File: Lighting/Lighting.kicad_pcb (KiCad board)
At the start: 2 copper layers, 70 x 65 mm, 72 parts, among them J1 USB_C_Receptacle, J2 USB_C_Receptacle, Q1 PSMN011, U1 MCP2210T-I_SO, U2 UTC2000-I_MG, U3 DAC8551IDGKT, U5 MCP1501_2v5, Y1 Crystal_12MHz

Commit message: gerber zip looks good to me
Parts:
- moved TP3 0.90 mm to (231.1, 120.9)
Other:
- board text added: "GND"
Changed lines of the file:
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@@
   (general
     (thickness 1.6)
-    (drawings 11)
+    (drawings 15)
     (tracks 567)
     (zones 0)
@@
   )
   (setup
-    (last_trace_width 0.25)
+    (last_trace_width 1.016)
     (user_trace_width 0.1524)
     (user_trace_width 0.2032)
@@
     (visible_elements 7FFFFFFF)
     (pcbplotparams
-      (layerselection 0x01000_7fffffff)
+      (layerselection 0x010f0_ffffffff)
       (usegerberextensions false)
       (usegerberattributes false)
@@
       (padsonsilk false)
       (subtractmaskfromsilk false)
-      (outputformat 4)
+      (outputformat 1)
       (mirror false)
-      (drillshape 2)
+      (drillshape 0)
       (scaleselection 1)
       (outputdirectory "Lighting_Fab/"))
@@
   (module wsolar:LED0805 (layer F.Cu)
     (at 237.758967 68.854171 90)
-    (fp_text reference D8 (at 0 -2.167 90) (layer F.SilkS)
+    (fp_text reference D8 (at -2.773829 -0.014967 180) (layer F.SilkS)
       (effects (font (size 1 1) (thickness 0.15)))
     )
@@
   (module wsolar:jumper_2 (layer F.Cu)
     (at 236.22 119.38)
-    (fp_text reference JP2 (at 0.635 2.54) (layer F.SilkS)
+    (fp_text reference JP2 (at 0 2.032) (layer F.SilkS)
       (effects (font (size 1 1) (thickness 0.15)))
     )
@@
   )
   (module wsolar:TP (layer F.Cu)
-    (at 232.029 120.777)
+    (at 231.14 120.904)
     (fp_text reference TP3 (at 0 -1.905) (layer F.SilkS)
       (effects (font (size 1 1) (thickness 0.15)))
@@
     (pad 20 smd rect (at 4.6 -5.715) (size 1.9 0.6) (layers F.Cu F.Paste F.Mask)
       (net 1 GND))
+  )
+  (gr_text GND (at 233.68 64.008 90) (layer F.SilkS)
+    (effects (font (size 1.27 1.27) (thickness 0.254)))
+  )
+  (gr_text GND (at 205.74 102.108) (layer F.SilkS)
+    (effects (font (size 1.5 1.5) (thickness 0.3)))
+  )
+  (gr_text GND (at 232.156 123.444) (layer F.SilkS)
+    (effects (font (size 1.27 1.27) (thickness 0.254)))
+  )
+  (gr_text GND (at 220.98 76.2) (layer F.SilkS)
+    (effects (font (size 1.5 1.5) (thickness 0.3)))
   )
   (gr_text "Wellesley Solar: Lighting Module v1" (at 233.68 92.583 45) (layer B.SilkS)
@@
   (segment (start 235.7374 81.805) (end 231.9214 81.805) (width 1.016) (layer F.Cu) (net 5))
   (segment (start 231.9214 81.805) (end 227.2534 86.473) (width 1.016) (layer F.Cu) (net 5))
-  (segment (start 235.7374 79.8322) (end 235.7374 81.805) (width 0.254) (layer F.Cu) (net 5))
-  (segment (start 229.3874 78.74) (end 234.6452 78.74) (width 0.254) (layer F.Cu) (net 5))
-  (segment (start 234.6452 78.74) (end 235.7374 79.8322) (width 0.254) (layer F.Cu) (net 5))
   (segment (start 235.218967 70.851033) (end 234.2388 71.8312) (width 0.254) (layer F.Cu) (net 5))
   (segment (start 235.218967 69.870171) (end 235.218967 70.851033) (width 0.254) (layer F.Cu) (net 5))
@@
   (segment (start 226.6696 78.232) (end 227.1776 78.74) (width 0.254) (layer F.Cu) (net 5))
   (segment (start 227.1776 78.74) (end 229.3874 78.74) (width 0.254) (layer F.Cu) (net 5))
+  (segment (start 229.3874 78.74) (end 234.6452 78.74) (width 1.016) (layer F.Cu) (net 5))
+  (segment (start 234.6452 78.74) (end 235.7374 79.8322) (width 1.016) (layer F.Cu) (net 5))
+  (segment (start 235.7374 79.8322) (end 235.7374 81.805) (width 1.016) (layer F.Cu) (net 5))
   (segment (start 247.019 105.1) (end 247.8532 105.9342) (width 0.254) (layer F.Cu) (net 6))
   (segment (start 246.04 105.1) (end 247.019 105.1) (width 0.254) (layer F.Cu) (net 6))
@@
     (polygon
       (pts
-        (xy 224.155 113.03) (xy 231.14 113.03) (xy 232.41 114.3) (xy 232.41 115.57) (xy 229.87 118.11)
-        (xy 229.7176 122.4788) (xy 224.0026 122.4788)
+        (xy 224.155 113.03) (xy 231.14 113.03) (xy 232.664 114.3) (xy 232.664 115.824) (xy 232.664 118.364)
+        (xy 232.664 122.428) (xy 224.0026 122.4788)
       )
     )

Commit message: changes based on feedback
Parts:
- removed C8: C_0u1, wsolar:C_0805
- removed D3, D4: LED_645nm, wsolar:LED0805
- removed JP4: Jumper_NO_Small, wsolar:jumper_2
- removed R10, R12, R8, R9: R_1k, wsolar:R0805
- removed R14, R15, R6, R7: R_10k, wsolar:R0805
- removed R17: R_39k4, wsolar:R0805
- removed U2: UTC2000-I_MG, wsolar:QFN50P300X300X90-17N
- D1, D2: value LED_645nm -> D_Zener_5v6; footprint wsolar:LED0805 -> wsolar:SOD123
- J2: value USB_C_Receptacle -> USB_B_Micro; footprint wsolar:MOLEX_105450-0101 -> wsolar:FCI_10118193-0001LF
- JP3: value Jumper_NO_Small -> Jumper_3; footprint wsolar:jumper_2 -> wsolar:jumper_3
- R4: value R_35k7 -> R_10k
- R5: value R_5k1 -> R_39k2
- U3: value DAC8551IDGKT -> DAC6551AQDGKRQ1; footprint wsolar:S-PDSO-G8 -> wsolar:SOP65P490X110-9N
- U4: value (none) -> LMC6482
- moved TP1 61.8 mm to (260.6, 70.6)
- moved D2 49.2 mm to (229.7, 105.3)
- moved R5 41.7 mm to (237.4, 117.9), turned to 180 degrees
- moved TP4 39.7 mm to (260.6, 78.1)
- moved TP2 32.2 mm to (260.6, 85.3)
- moved R4 29.9 mm to (237.6, 106.5), turned to 270 degrees
- moved D1 24.6 mm to (261.8, 101.6), turned to 90 degrees
- moved JP1 22.3 mm to (227.8, 96.0), turned to 270 degrees
- moved R1 19.0 mm to (231.8, 99.7)
- moved TP3 18.0 mm to (249.2, 121.2)
- moved R3 16.9 mm to (245.0, 70.6), turned to 270 degrees
- moved C5 13.6 mm to (251.3, 100.3), turned to 270 degrees
- moved R11 11.6 mm to (224.2, 77.5), turned to 0 degrees
- moved C9 7.53 mm to (248.9, 108.5), turned to 0 degrees
- moved R16 7.03 mm to (256.5, 101.6)
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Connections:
- D1 pad 2: Net-(D1-Pad2) -> GND
- D2 pad 2: Net-(D2-Pad2) -> GND
- J1 pad A10: Net-(J1-PadA10) -> (no net)
- J1 pad A11: Net-(J1-PadA11) -> (no net)
- J1 pad A2: Net-(J1-PadA2) -> (no net)
- J1 pad A3: Net-(J1-PadA3) -> (no net)
- J1 pad A6: Net-(J1-PadA6) -> (no net)
- J1 pad A7: Net-(J1-PadA7) -> (no net)
- J1 pad A8: Net-(J1-PadA8) -> (no net)
- J1 pad B10: Net-(J1-PadB10) -> (no net)
- J1 pad B11: Net-(J1-PadB11) -> (no net)
- J1 pad B2: Net-(J1-PadB2) -> (no net)
- J1 pad B3: Net-(J1-PadB3) -> (no net)
- J1 pad B6: Net-(J1-PadB6) -> (no net)
- J1 pad B7: Net-(J1-PadB7) -> (no net)
- J1 pad B8: Net-(J1-PadB8) -> (no net)
- JP3 pad 1: Net-(JP3-Pad1) -> Net-(D2-Pad1)
- R16 pad 2: Net-(J2-PadA4) -> Net-(D1-Pad1)
- R2 pad 1: Net-(J1-PadA5) -> Net-(J1-PadB5)
- R3 pad 1: Net-(J1-PadB5) -> Net-(J1-PadA5)
- R4 pad 1: Net-(C6-Pad1) -> Net-(JP3-Pad2)
- R4 pad 2: Net-(R4-Pad2) -> GND
- R5 pad 1: Net-(R4-Pad2) -> VCC
- R5 pad 2: GND -> Net-(JP2-Pad1)
- RV1 pad 2: Net-(JP3-Pad1) -> Net-(JP3-Pad3)
- TP3 pad 1: GND -> VCC
- U1 pad 10: Net-(U1-Pad10) -> (no net)
- U1 pad 12: Net-(U1-Pad12) -> (no net)
- U1 pad 13: Net-(U1-Pad13) -> (no net)
- U1 pad 14: Net-(U1-Pad14) -> (no net)
- U1 pad 15: Net-(U1-Pad15) -> (no net)
- U1 pad 5: Net-(U1-Pad5) -> (no net)
- U1 pad 6: Net-(U1-Pad6) -> (no net)
- U1 pad 7: Net-(U1-Pad7) -> (no net)
- U3 pad 3: Net-(JP4-Pad1) -> Net-(JP3-Pad2)
- U3 pad 4: Net-(JP4-Pad1) -> Net-(JP3-Pad2)
- U4 pad 3: Net-(JP3-Pad2) -> Net-(D2-Pad1)
- U4 pad 7: Net-(U4-Pad7) -> (no net)
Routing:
- net VCC: track 241.9 -> 158.3 mm
- net Net-(JP4-Pad1): track 16.4 -> 0.00 mm
- net Net-(J2-PadA4): track 15.5 -> 0.00 mm, vias 2 -> 0
- net /D+: track 37.5 -> 22.1 mm
- net Net-(J1-PadA5): track 17.5 -> 2.43 mm, vias 2 -> 0
- net +5V: track 48.7 -> 35.1 mm
- net Net-(J1-PadB5): track 21.1 -> 8.93 mm
- net Net-(D2-Pad1): track 7.44 -> 19.3 mm
- net Net-(JP3-Pad3): track 0.00 -> 11.5 mm
- net Net-(R4-Pad2): track 9.71 -> 0.00 mm
- net Net-(C12-Pad1): track 14.0 -> 22.0 mm
- net Net-(D3-Pad1): track 6.82 -> 0.00 mm
- net Net-(C6-Pad1): track 60.5 -> 54.3 mm, vias 2 -> 0
- net Net-(C5-Pad1): track 14.3 -> 8.78 mm
- net Net-(JP3-Pad1): track 5.21 -> 0.00 mm
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- removed copper zone on F.Cu, net +5V
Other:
- board text added: "---> ext LED pwr"
- board text added: "<-Dimmer Brighter->"
- board text added: "DAC"
- board text added: "LED Current Probe ->"
- board text added: "LED Power Indicator"
- board text added: "POT"
- board text added: "USB to Computer"
- board text added: "USB-C for LED"
- board text added: "USB-SPI Reset Active Low"
- board text added: "Vcc Power Indicator"
- board text added: "wave gen->"

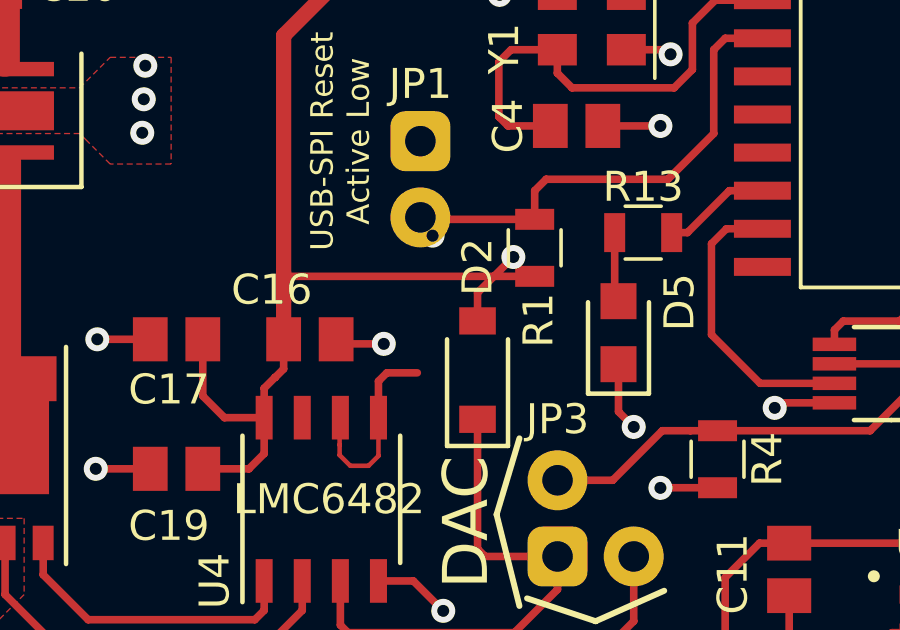
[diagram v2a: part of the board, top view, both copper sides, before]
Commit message: minor trace fix; add readme
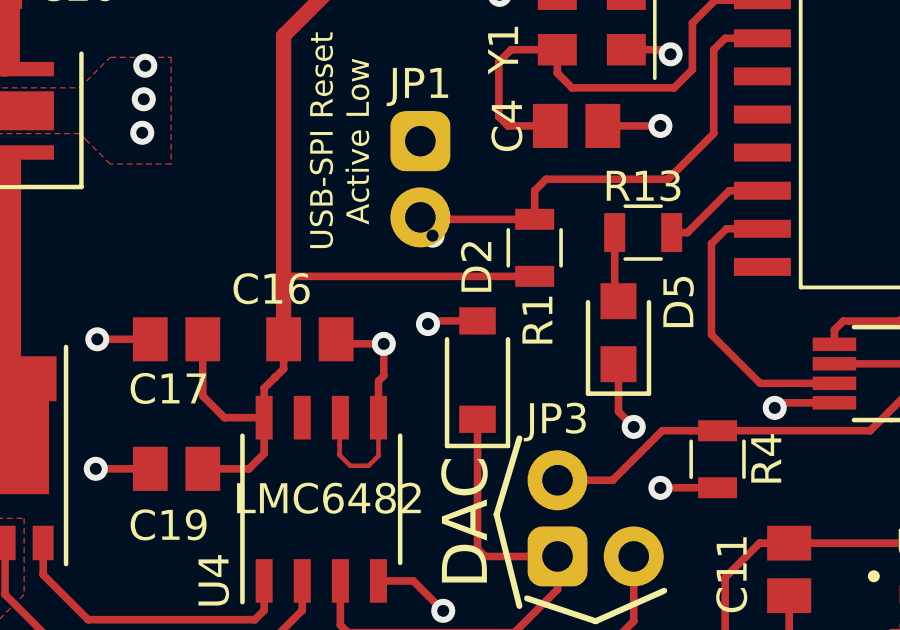
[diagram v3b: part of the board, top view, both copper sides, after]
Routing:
- net GND: track 107.8 -> 106.8 mm
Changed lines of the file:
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@@
   )
   (setup
-    (last_trace_width 0.254)
+    (last_trace_width 0.25)
     (user_trace_width 0.1524)
     (user_trace_width 0.2032)
@@
   (segment (start 226.441 106.5022) (end 226.441 105.228652) (width 0.1524) (layer F.Cu) (net 1) (status 20))
   (segment (start 226.1108 106.8324) (end 226.441 106.5022) (width 0.1524) (layer F.Cu) (net 1))
-  (via (at 228.2444 99.1616) (size 0.8) (drill 0.4) (layers F.Cu B.Cu) (net 17))
   (via (at 217.0684 102.616) (size 0.8) (drill 0.4) (layers F.Cu B.Cu) (net 1))
   (via (at 217.0176 106.934) (size 0.8) (drill 0.4) (layers F.Cu B.Cu) (net 1))
@@
   (segment (start 241.68 66.478) (end 240.79 67.368) (width 0.25) (layer F.Cu) (net 1) (status 30))
   (segment (start 242.01 66.478) (end 241.68 66.478) (width 0.25) (layer F.Cu) (net 1) (status 30))
-  (segment (start 226.7204 103.7336) (end 227.7364 103.7336) (width 0.254) (layer F.Cu) (net 1))
   (segment (start 226.441 105.228652) (end 226.441 104.013) (width 0.254) (layer F.Cu) (net 1) (status 10))
-  (segment (start 226.441 104.013) (end 226.7204 103.7336) (width 0.254) (layer F.Cu) (net 1))
   (segment (start 225.1824 102.7684) (end 225.03 102.616) (width 0.254) (layer F.Cu) (net 1) (status 30))
   (segment (start 226.6188 102.7684) (end 225.1824 102.7684) (width 0.254) (layer F.Cu) (net 1) (status 20))
@@
   (segment (start 240.1316 111.1618) (end 240.1316 112.3696) (width 0.254) (layer F.Cu) (net 1))
   (segment (start 240.1316 112.3696) (end 240.4872 112.7252) (width 0.254) (layer F.Cu) (net 1))
-  (via (at 230.9368 99.8728) (size 0.8) (drill 0.4) (layers F.Cu B.Cu) (net 1))
-  (segment (start 229.743 102.003) (end 229.743 101.0666) (width 0.254) (layer F.Cu) (net 1))
-  (segment (start 229.743 101.0666) (end 230.9368 99.8728) (width 0.254) (layer F.Cu) (net 1))
   (via (at 258.318 91.4908) (size 0.8) (drill 0.4) (layers F.Cu B.Cu) (net 1))
   (segment (start 256.766 91.44) (end 258.2672 91.44) (width 0.254) (layer F.Cu) (net 1))
@@
   (segment (start 232.17 90.881) (end 232.403 91.114) (width 0.254) (layer F.Cu) (net 1))
   (segment (start 232.17 88.519) (end 232.17 90.881) (width 0.254) (layer F.Cu) (net 1))
+  (segment (start 226.6188 103.8352) (end 226.441 104.013) (width 0.25) (layer F.Cu) (net 1))
+  (segment (start 226.6188 102.7684) (end 226.6188 103.8352) (width 0.25) (layer F.Cu) (net 1))
+  (via (at 228.092 102.108) (size 0.8) (drill 0.4) (layers F.Cu B.Cu) (net 1))
+  (segment (start 229.743 102.003) (end 228.197 102.003) (width 0.25) (layer F.Cu) (net 1))
+  (segment (start 228.197 102.003) (end 228.092 102.108) (width 0.25) (layer F.Cu) (net 1))
   (segment (start 237.617 90.043) (end 239.24 90.043) (width 0.254) (layer F.Cu) (net 2))
   (segment (start 236.546 91.114) (end 237.617 90.043) (width 0.254) (layer F.Cu) (net 2))
@@
   (segment (start 248.44 90.043) (end 249.936 90.043) (width 0.254) (layer F.Cu) (net 16))
   (segment (start 249.936 90.043) (end 251.714 91.821) (width 0.254) (layer F.Cu) (net 16))
+  (via (at 228.2444 99.1616) (size 0.8) (drill 0.4) (layers F.Cu B.Cu) (net 17))
   (segment (start 231.648 97.663) (end 231.648 98.618) (width 0.254) (layer F.Cu) (net 17))
   (segment (start 237.998 92.583) (end 237.617 92.964) (width 0.254) (layer F.Cu) (net 17))
